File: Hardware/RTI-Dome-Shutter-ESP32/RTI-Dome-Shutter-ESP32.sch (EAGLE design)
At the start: 65 parts, among them IC1 REG1117FA-5.0_500, IC2 24LC64T-I/SN, IC8 REG1117-3.3V, J1 691313510003, J10 691313510002, J11 691313510002, J12 691313510002, J2 XT60PW-M, J3 691313510003, J4 691313510003, J6 691313510003, J7 691313510003, J8 691313510002, J9 691313510002, U1 ESP32-DevKitC ESP32-WROOM-32U

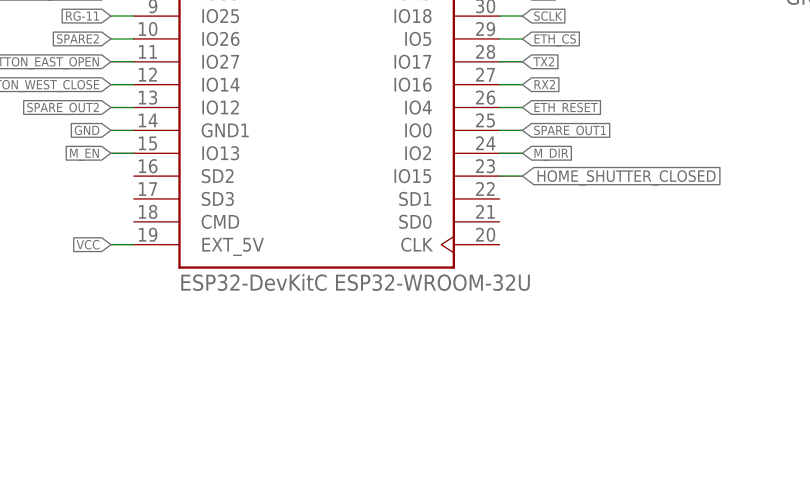
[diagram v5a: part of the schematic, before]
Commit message: Fix components orientation in the library to match JLCPCB
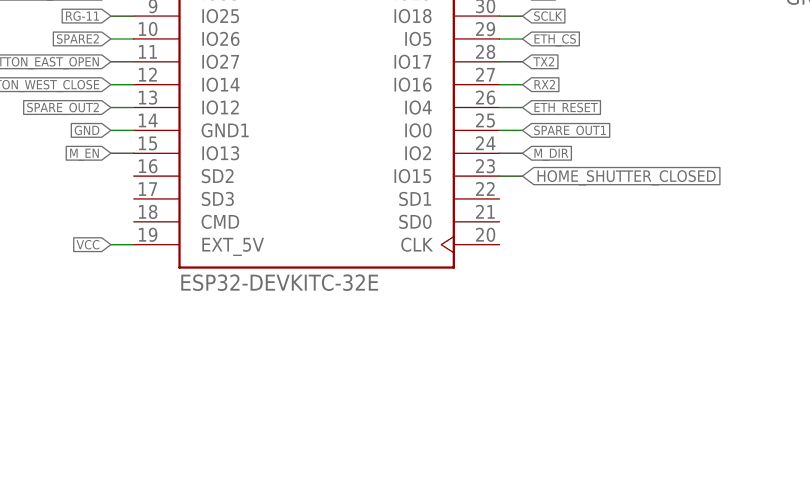
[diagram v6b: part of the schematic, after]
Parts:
- U1: value ESP32-DevKitC ESP32-WROOM-32U -> ESP32-DEVKITC-32E
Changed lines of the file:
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@@
 <part name="JP1" library="rti" library_urn="urn:adsk.eagle:library:37256580" deviceset="JP2E" device="" package3d_urn="urn:adsk.eagle:package:37318384/1"/>
 <part name="GND6" library="supply1" library_urn="urn:adsk.eagle:library:371" deviceset="GND" device=""/>
-<part name="U1" library="ESP32-DEVKITC-32D" library_urn="urn:adsk.eagle:library:44270575" deviceset="ESP32-DEVKITC-32" device="D" package3d_urn="urn:adsk.eagle:package:44270578/5" value="ESP32-DevKitC ESP32-WROOM-32U"/>
+<part name="U1" library="ESP32-DEVKITC-32D" library_urn="urn:adsk.eagle:library:44270575" deviceset="ESP32-DEVKITC-32" device="D" package3d_urn="urn:adsk.eagle:package:44270578/5" value="ESP32-DEVKITC-32E"/>
 <part name="J1" library="samacsys" library_urn="urn:adsk.eagle:library:37256869" deviceset="691313510003" device="" package3d_urn="urn:adsk.eagle:package:45454765/2"/>
 <part name="J3" library="samacsys" library_urn="urn:adsk.eagle:library:37256869" deviceset="691313510003" device="" package3d_urn="urn:adsk.eagle:package:45454765/2"/>
